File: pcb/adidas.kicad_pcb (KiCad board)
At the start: 2 copper layers, 152.7 x 107.2 mm, 43 parts, among them J1 ISP Header, J2 Shitty Add-on, J3 Conn_01x04_Pin, J4 Battery, U1 MPU-6050, U2 ATTINY841-SSU

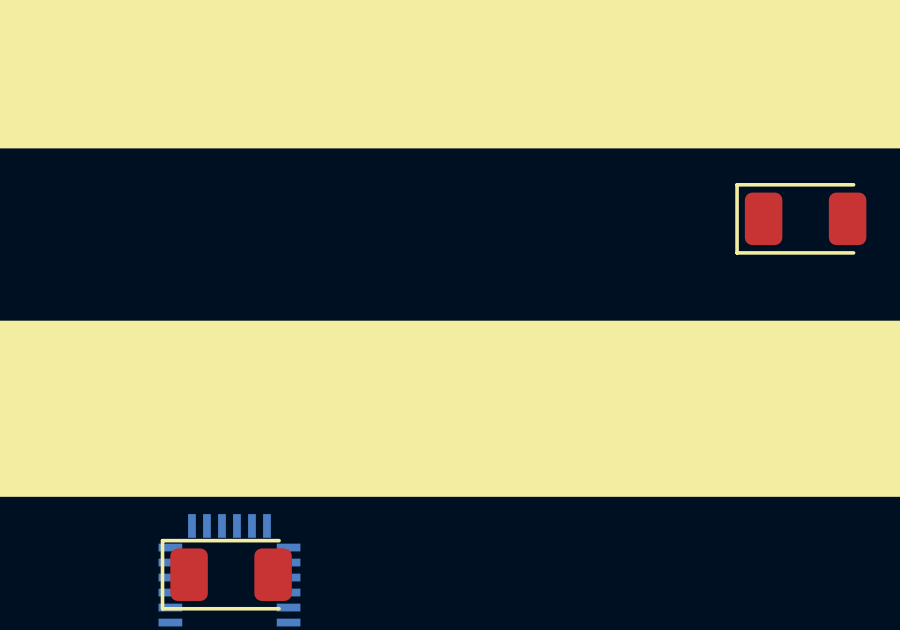
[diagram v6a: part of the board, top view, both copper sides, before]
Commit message: update back of board
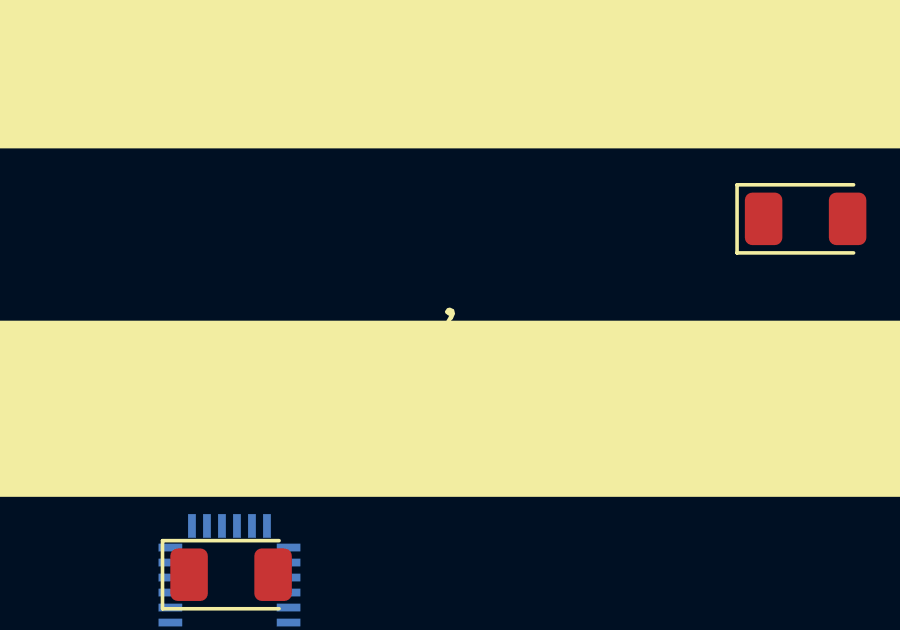
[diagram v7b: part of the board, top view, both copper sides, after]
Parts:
- moved APPLE2 2.27 mm to (227.7, 105.8)
- moved comm 0.16 mm to (227.7, 104.0)
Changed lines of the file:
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@@
   (net 38 "unconnected-(U2-PA2-Pad11)")
   (footprint "DEAD10C5:apple2" (layer "F.Cu")
-    (at 228.8032 103.8352)
+    (at 227.6856 105.8164)
     (attr board_only exclude_from_pos_files exclude_from_bom)
     (fp_text reference "APPLE2" (at 0 -2.54) (layer "Cmts.User") hide
@@
   )
   (footprint "DEAD10C5:comma" (layer "F.Cu")
-    (at 227.584 104.0384)
+    (at 227.7364 103.9876)
     (attr board_only exclude_from_pos_files exclude_from_bom)
     (fp_text reference "comm" (at 0 -1.27) (layer "Cmts.User") hide
@@
       (pts
         (xy 0.134229 0.401972)
-        (xy 0.168916 0.548366)
-        (xy 0.094028 0.718796)
-        (xy 0.06796 0.747559)
-        (xy -0.058609 0.837596)
-        (xy -0.130832 0.834901)
-        (xy -0.104125 0.746906)
-        (xy -0.08495 0.722074)
-        (xy -0.028089 0.616518)
-        (xy -0.074548 0.594649)
-        (xy -0.159076 0.526013)
-        (xy -0.1699 0.467224)
-        (xy -0.099078 0.36345)
-        (xy 0 0.339799)
+        (xy 0.099542 0.548366)
+        (xy 0.17443 0.718796)
+        (xy 0.200498 0.747559)
+        (xy 0.327067 0.837596)
+        (xy 0.39929 0.834901)
+        (xy 0.372583 0.746906)
+        (xy 0.353408 0.722074)
+        (xy 0.296547 0.616518)
+        (xy 0.343006 0.594649)
+        (xy 0.427534 0.526013)
+        (xy 0.438358 0.467224)
+        (xy 0.367536 0.36345)
+        (xy 0.268458 0.339799)
       )
       (stroke (width 0) (type solid)) (fill solid) (layer "B.SilkS"))
@@
     (at 231.6988 103.886)
     (attr board_only exclude_from_pos_files exclude_from_bom)
-    (fp_text reference "G***" (at 0 -1.27 360) (layer "Cmts.User") hide
+    (fp_text reference "G***" (at 0 -1.27) (layer "Cmts.User") hide
       (effects (font (size 1.5 1.5) (thickness 0.3)))
     )
-    (fp_text value "LOGO" (at 0 1.27 360) (layer "Cmts.User") hide
+    (fp_text value "LOGO" (at 0 1.27) (layer "Cmts.User") hide
       (effects (font (size 1.5 1.5) (thickness 0.3)))
     )
@@
     (at 230.3272 104.14)
     (attr board_only exclude_from_pos_files exclude_from_bom)
-    (fp_text reference "G***" (at 0 -1.27 360) (layer "Cmts.User") hide
+    (fp_text reference "G***" (at 0 -1.27) (layer "Cmts.User") hide
       (effects (font (size 1.5 1.5) (thickness 0.3)))
     )
-    (fp_text value "LOGO" (at 0.75 2.54 360) (layer "Cmts.User") hide
+    (fp_text value "LOGO" (at 0.75 2.54) (layer "Cmts.User") hide
       (effects (font (size 1.5 1.5) (thickness 0.3)))
     )
@@
     (at 172.72 119.38 180)
     (attr board_only exclude_from_pos_files exclude_from_bom)
-    (fp_text reference "G***" (at 0 0 -180) (layer "B.SilkS") hide
-      (effects (font (size 1.5 1.5) (thickness 0.3)) (justify mirror))
+    (fp_text reference "G***" (at 0 1.27 180) (layer "Cmts.User") hide
+      (effects (font (size 1.5 1.5) (thickness 0.3)))
     )
-    (fp_text value "LOGO" (at 0.75 0 -180) (layer "B.SilkS") hide
-      (effects (font (size 1.5 1.5) (thickness 0.3)) (justify mirror))
+    (fp_text value "LOGO" (at 0.75 -2.54 180) (layer "Cmts.User") hide
+      (effects (font (size 1.5 1.5) (thickness 0.3)))
     )
     (fp_poly
       (pts
         (xy 0.134229 -0.401972)
-        (xy 0.168916 -0.548366)
-        (xy 0.094028 -0.718796)
-        (xy 0.06796 -0.747559)
-        (xy -0.058609 -0.837596)
-        (xy -0.130832 -0.834901)
-        (xy -0.104125 -0.746906)
-        (xy -0.08495 -0.722074)
-        (xy -0.028089 -0.616518)
-        (xy -0.074548 -0.594649)
-        (xy -0.159076 -0.526013)
-        (xy -0.1699 -0.467224)
-        (xy -0.099078 -0.36345)
-        (xy 0 -0.339799)
+        (xy 0.099542 -0.548366)
+        (xy 0.17443 -0.718796)
+        (xy 0.200498 -0.747559)
+        (xy 0.327067 -0.837596)
+        (xy 0.39929 -0.834901)
+        (xy 0.372583 -0.746906)
+        (xy 0.353408 -0.722074)
+        (xy 0.296547 -0.616518)
+        (xy 0.343006 -0.594649)
+        (xy 0.427534 -0.526013)
+        (xy 0.438358 -0.467224)
+        (xy 0.367536 -0.36345)
+        (xy 0.268458 -0.339799)
       )
-      (stroke (width 0) (type solid)) (fill solid) (layer "B.SilkS"))
+      (stroke (width 0) (type solid)) (fill solid) (layer "F.SilkS"))
   )
   (footprint "Resistor_SMD:R_1206_3216Metric" (layer "B.Cu")

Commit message: work on puzzle
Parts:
- removed the APPLE2 at (227.7, 105.8)
- removed G***: LOGO, DEAD10C5:melon
- removed G***: LOGO, DEAD10C5:olive
- removed G***: LOGO, DEAD10C5:comma
- removed the comm at (227.7, 104.0)
- added APPLE2: LOGO, DEAD10C5:apple2, F.Cu at (202.7, 104.1)
- added APPLE2: LOGO, DEAD10C5:apple2, F.Cu at (200.2, 104.2)
- added APPLE2: LOGO, DEAD10C5:apple2, F.Cu at (217.7, 104.1)
- added APPLE2: LOGO, DEAD10C5:apple2, F.Cu at (204.5, 104.1)
- added APPLE2: LOGO, DEAD10C5:apple2, F.Cu at (201.4, 104.2)
- added APPLE2: LOGO, DEAD10C5:apple2, F.Cu at (212.9, 104.1)
- added APPLE2: LOGO, DEAD10C5:apple2, F.Cu at (191.8, 104.2)
- added APPLE2: LOGO, DEAD10C5:apple2, F.Cu at (194.3, 104.2)
- added APPLE2: LOGO, DEAD10C5:apple2, F.Cu at (220.2, 104.0)
- added APPLE2: LOGO, DEAD10C5:apple2, F.Cu at (210.0, 104.1)
- added APPLE2: LOGO, DEAD10C5:apple2, F.Cu at (193.0, 104.2)
- added comm: LOGO, DEAD10C5:comma, F.Cu at (203.5, 104.3)
- added comm: LOGO, DEAD10C5:comma, F.Cu at (209.0, 104.2)
- added comm: LOGO, DEAD10C5:comma, F.Cu at (197.9, 104.3)
- added comm: LOGO, DEAD10C5:comma, F.Cu at (216.5, 104.2)
- added comm: LOGO, DEAD10C5:comma, F.Cu at (190.7, 104.4)
- added comm: LOGO, DEAD10C5:comma, F.Cu at (224.0, 104.2)
- added melon1: melon, DEAD10C5:melon, F.Cu at (205.7, 104.2)
- added melon1: melon, DEAD10C5:melon, F.Cu at (219.0, 104.2)
- added melon1: melon, DEAD10C5:melon, F.Cu at (231.2, 104.0)
- added melon1: melon, DEAD10C5:melon, F.Cu at (223.4, 104.1)
- added melon1: melon, DEAD10C5:melon, F.Cu at (199.0, 104.3)
- added melon1: melon, DEAD10C5:melon, F.Cu at (215.9, 104.1)
- added melon1: melon, DEAD10C5:melon, F.Cu at (226.9, 104.0)
- added melon1: melon, DEAD10C5:melon, F.Cu at (208.5, 104.2)
- added melon1: melon, DEAD10C5:melon, F.Cu at (197.2, 104.3)
- added olive: LOGO, DEAD10C5:olive, F.Cu at (221.8, 104.2)
- added olive: LOGO, DEAD10C5:olive, F.Cu at (228.3, 104.1)
- added olive: LOGO, DEAD10C5:olive, F.Cu at (225.4, 104.1)
- added olive: LOGO, DEAD10C5:olive, F.Cu at (195.7, 104.4)
- added olive: LOGO, DEAD10C5:olive, F.Cu at (214.4, 104.2)
- added olive: LOGO, DEAD10C5:olive, F.Cu at (211.5, 104.3)
- added olive: LOGO, DEAD10C5:olive, F.Cu at (207.1, 104.3)
- added olive: LOGO, DEAD10C5:olive, F.Cu at (229.9, 104.1)
- moved U1 0.53 mm to (164.8, 129.4)
